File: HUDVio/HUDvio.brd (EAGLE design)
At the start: 85 x 54 mm, 53 parts, among them U1 ST_STM32F446RET7, U3 TVP5150AM1PBSR, U4 NEXPERIA_NVT2006, U5 MAXIM_MAX4389, X1 ABRACON_ABM8-27.000MHZ, X2 ABRACON_ABM8-14.31818MHZ

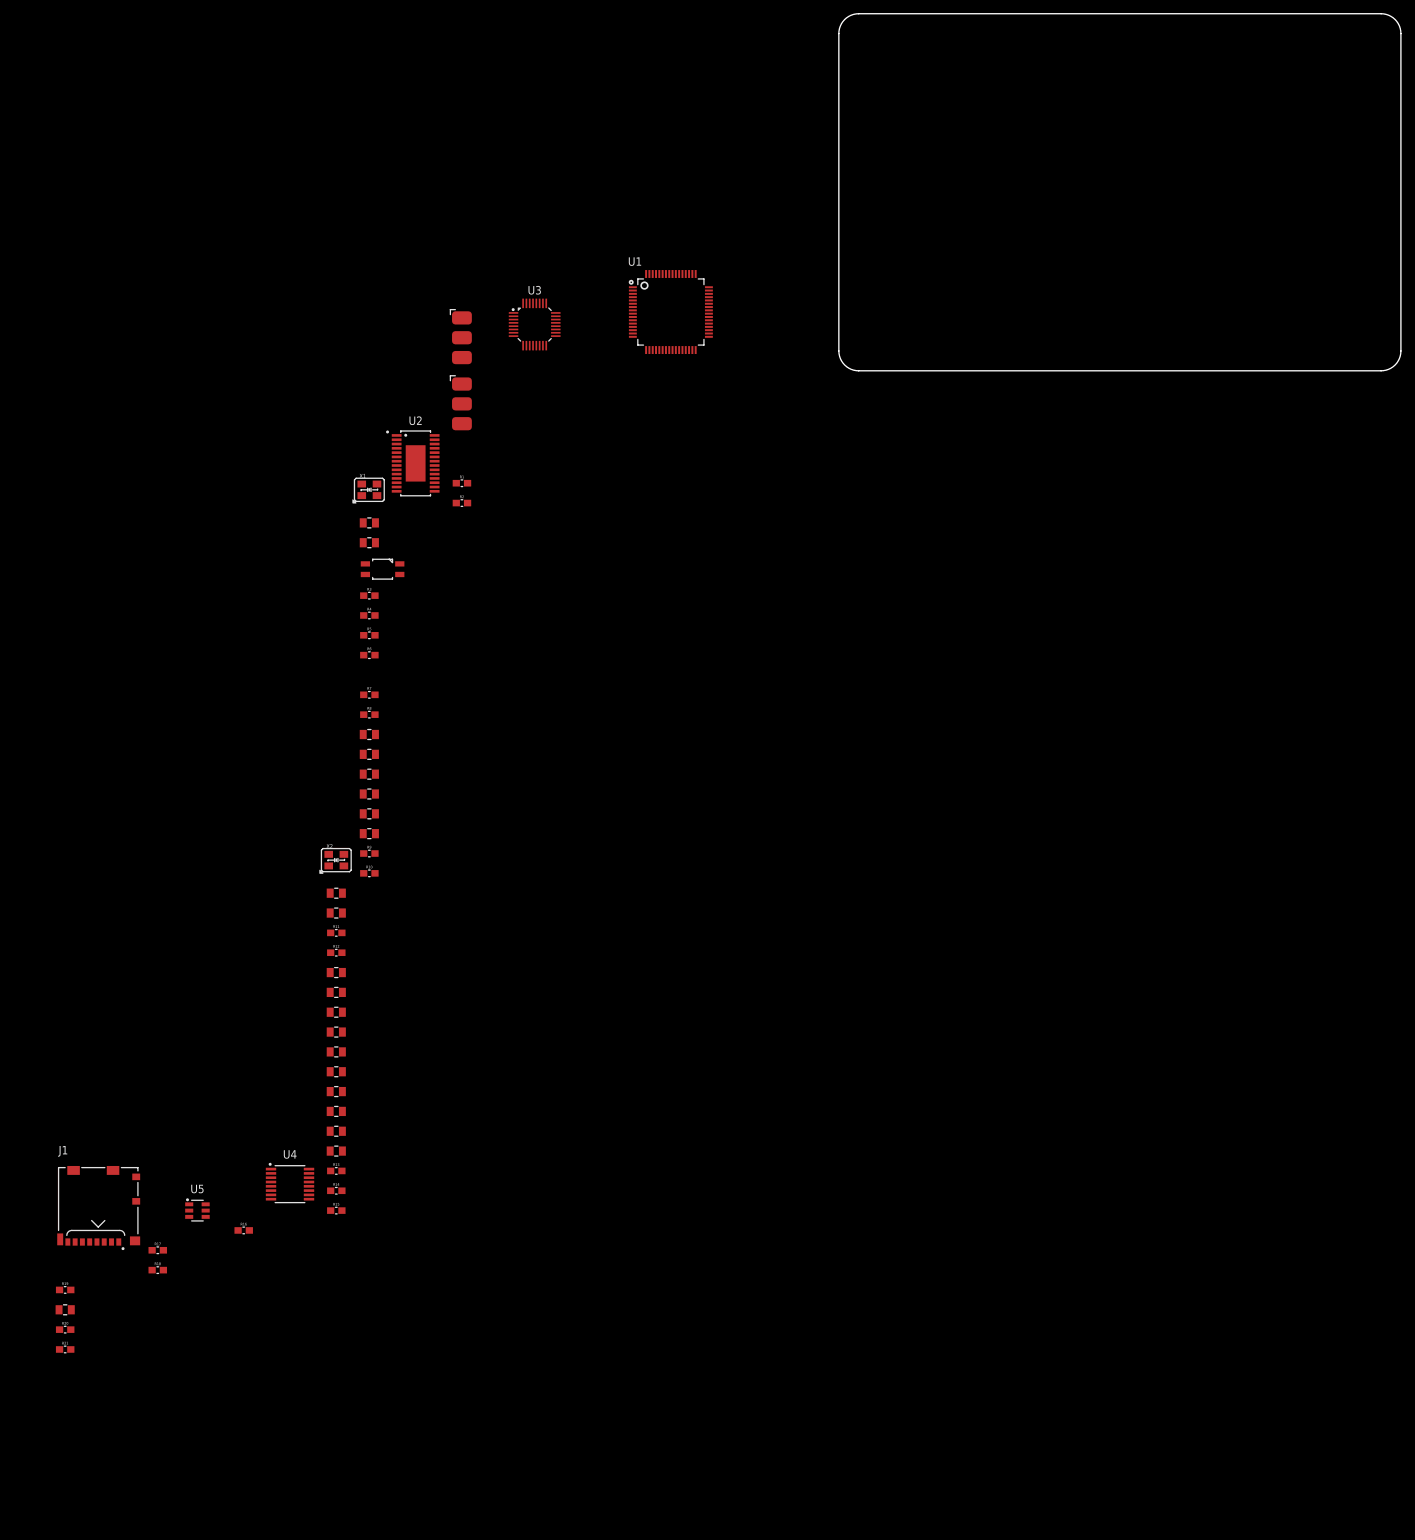
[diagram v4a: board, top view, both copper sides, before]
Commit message: Added 3rd sheet
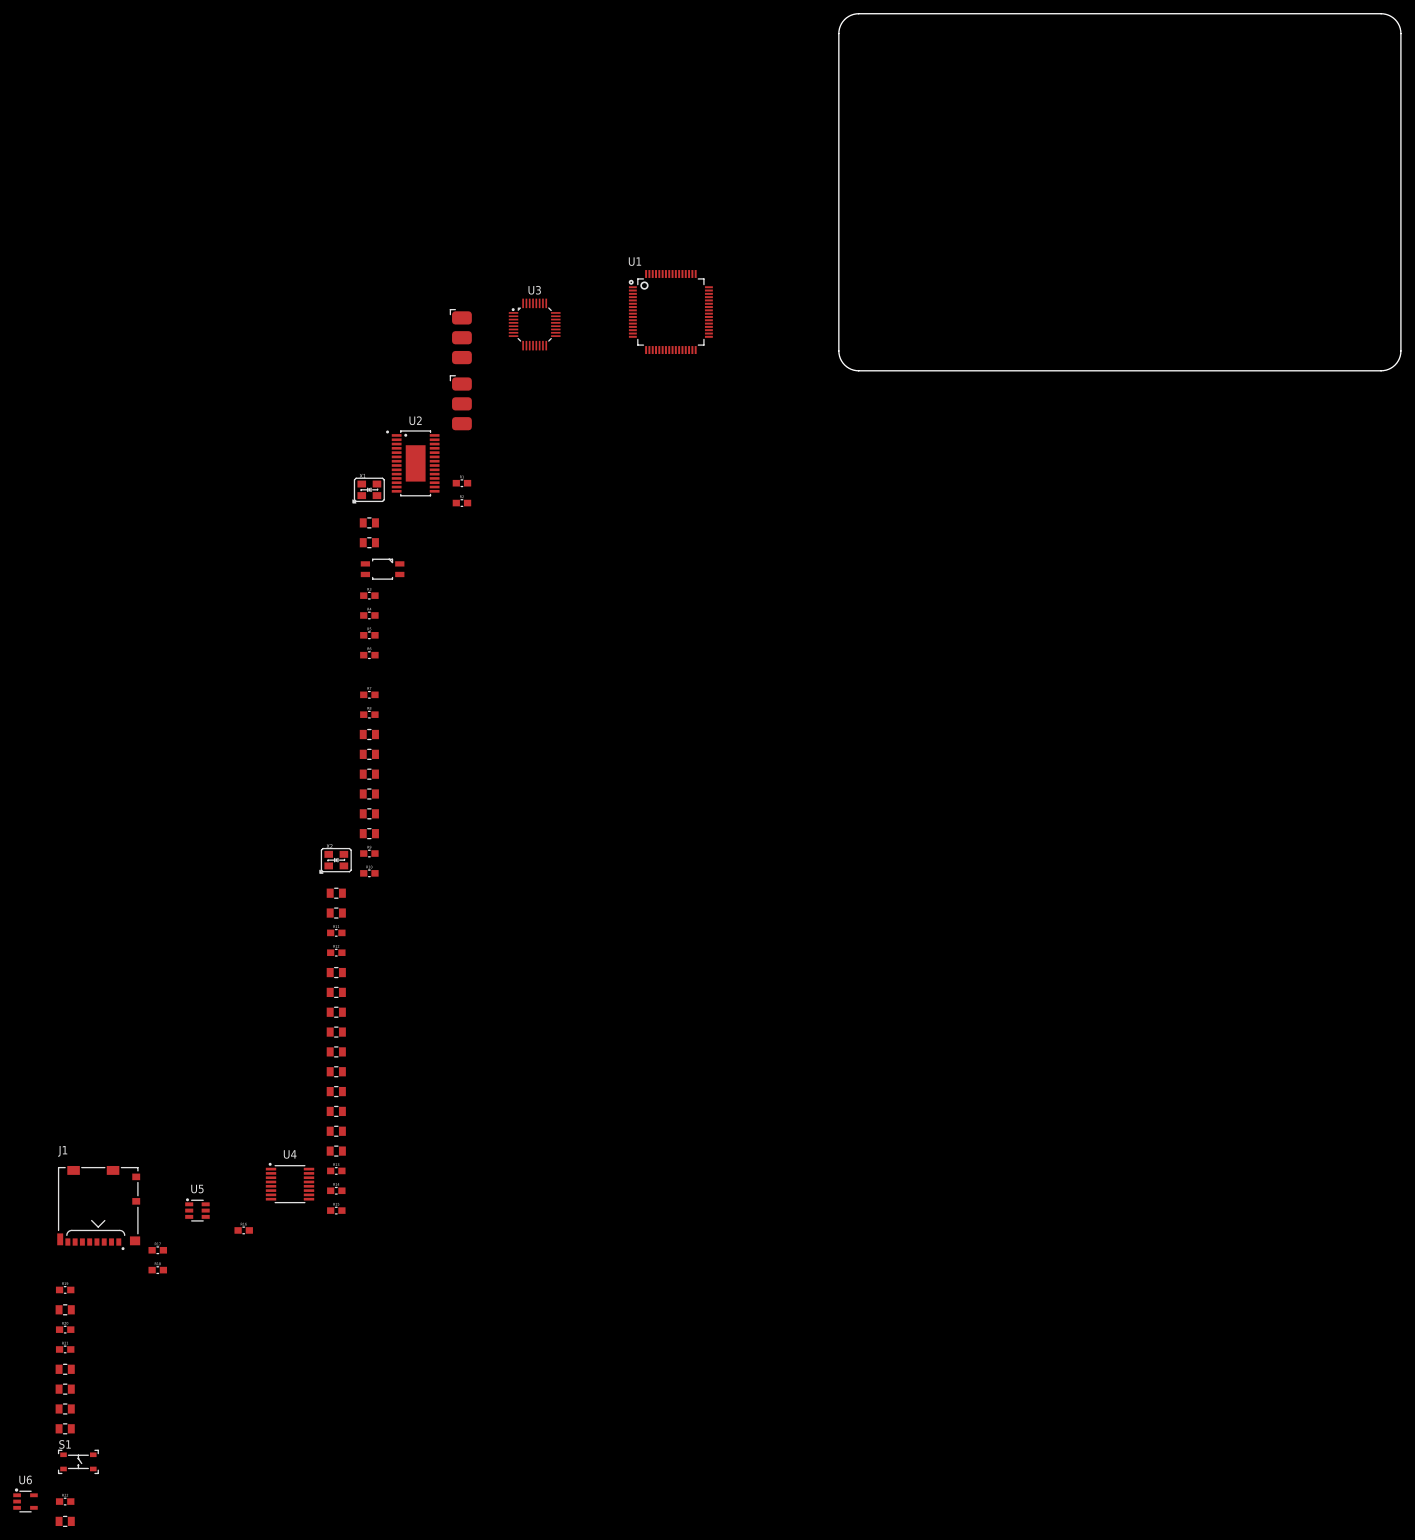
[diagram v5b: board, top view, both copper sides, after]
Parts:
- added C22, C23, C24, C25, C26: 1UF_0805, Skyhawkson-Capacitors:KEMET_0805
- added R22: 1K_0603, Skyhawkson-Resistors:0603
- added S1: C&K_PTS815, Skyhawkson-Miscellaneous:C&K_PTS815
- added U6: MIC_MIC5504-1.8, Skyhawkson-Power:MIC_SOT23-5LD-PL-1
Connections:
- removed net GNDA/VREF-: U1.12
- removed net VDD: U1.19, U1.32, U1.48, U1.64
- new net N$16: S1.2, U1.7
- new net N$17: R22.1, S1.1
- new net N$18: C26.P$2, S1.3
- new net VIN: U6.1
- new net VOUT: U6.5
- net +3V3: now also C22.P$1, C23.P$1, C24.P$1, C25.P$1, C26.P$1, R22.2, U1.13, U1.19, U1.32, U1.48, U1.64
- net 5150-CS: now also U1.33
- net BLU: now also U1.16
- net GND: now also C22.P$2, C23.P$2, C24.P$2, C25.P$2, S1.4, U1.12, U6.2
- net GRE: now also U1.15
- net LOS-LV: now also U1.8
- net MISO-LV: now also U1.35
- net MOSI-LV: now also U1.36
- net RED: now also U1.14
- net SCL: now also U1.29
- net SCLK-LV: now also U1.34
- net SD-CS: now also U1.56
- net SDA: now also U1.55
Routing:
- added copper zone on layer 2, net GND

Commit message: Schematic done, moving to Board
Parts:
- added C27, C28, C29, C30, C31, C32: 1UF_0805, Skyhawkson-Capacitors:KEMET_0805
- added J2: PHOENIX_SPTAF1/2-3,5, Skyhawkson-Connectors:PHOENIX_SPTAF1/X-3,5
- added U7: TOR_XC6220B331, Skyhawkson-Power:TOR_SOT-25
- added U8: ROHM_BD50HC5WEFJ, Skyhawkson-Power:ROHM_HTSOP-J8
- moved U$3 147.4 mm to (83.0, 41.0)
- moved U$1 69.1 mm to (2.00, 41.0)
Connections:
- removed net VIN: U6.1
- removed net VOUT: U6.5
- new net N$19: C29.P$1, C30.P$1, U7.2
- net +1V8: now also C28.P$2, U6.5
- net +3V3: now also C29.P$2, U7.5
- net +5V: now also C27.P$2, C30.P$2, C32.P$1, C32.P$2, U6.1, U6.3, U7.1, U7.3, U8.1, U8.2
- net GND: now also C27.P$1, C28.P$1, C31.P$1, C31.P$2, J2.1@BACK, J2.1@FRONT, J2.2@BACK, J2.2@FRONT, U8.3, U8.5, U8.8, U8.FIN, U8.FIN10, U8.FIN11, U8.FIN14, U8.FIN20, U8.FIN21, U8.FIN22, U8.FIN23, U8.FIN24, U8.FIN30, U8.FIN31, U8.FIN33, U8.FIN34

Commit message: Schematic Complete
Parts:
- added U$30: SWD_HEADER, Skyhawkson-Connectors:CNC_3220-10-0300-00
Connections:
- removed net N$16: S1.2, U1.7
- new net !RST: S1.2, U$30.10, U1.7
- new net SWCLK: U$30.4, U1.49
- new net SWDIO: U$30.2, U1.46
- net +3V3: now also U$30.1
- net GND: now also U$30.3, U$30.5, U$30.9
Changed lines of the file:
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@@
 <attribute name="VAL" value="1uF" x="-165" y="-192" size="1.778" layer="27" display="off"/>
+</element>
+<element name="U$30" library="Skyhawkson-Connectors" library_urn="urn:adsk.eagle:library:23896875" package="CNC_3220-10-0300-00" package3d_urn="urn:adsk.eagle:package:26105697/4" value="SWD_HEADER" x="-160" y="-199" smashed="yes">
+<attribute name="DKPN" value="1175-1629-ND" x="-160" y="-199" size="1.778" layer="27" display="off"/>
+<attribute name="NAME" x="-167" y="-195" size="1.27" layer="25"/>
+<attribute name="VALUE" x="-167" y="-203.5" size="1.27" layer="27" align="top-left"/>
 </element>
 </elements>
@@
 <contactref element="U8" pad="FIN33"/>
 <contactref element="C31" pad="P$2"/>
+<contactref element="U$30" pad="5"/>
+<contactref element="U$30" pad="3"/>
+<contactref element="U$30" pad="9"/>
 <wire x1="-114.395" y1="-131.75" x2="-117.755" y2="-131.35" width="0" layer="19" extent="1-1"/>
 <wire x1="-117.85" y1="-139" x2="-117.755" y2="-131.35" width="0" layer="19" extent="1-1"/>
@@
 <wire x1="-164.075" y1="-189" x2="-158.75" y2="-181.5" width="0" layer="19" extent="1-1"/>
 <wire x1="-165.925" y1="-189" x2="-164.075" y2="-189" width="0" layer="19" extent="1-1"/>
+<wire x1="-161.27" y1="-201.015" x2="-164.075" y2="-189" width="0" layer="19" extent="1-1"/>
+<wire x1="-160" y1="-201.015" x2="-161.27" y2="-201.015" width="0" layer="19" extent="1-1"/>
+<wire x1="-157.46" y1="-201.015" x2="-160" y2="-201.015" width="0" layer="19" extent="1-1"/>
 <wire x1="-70.075" y1="-26" x2="-70.15" y2="-49" width="0" layer="19" extent="1-1"/>
 <wire x1="-70.075" y1="-23" x2="-70.075" y2="-26" width="0" layer="19" extent="1-1"/>
@@
 <wire x1="-61.1265" y1="-13.025" x2="-66.8735" y2="-11.725" width="0" layer="19" extent="1-1"/>
 <wire x1="-61.1265" y1="-14.975" x2="-61.1265" y2="-13.025" width="0" layer="19" extent="1-1"/>
-<wire x1="83" y1="41" x2="-61.1265" y2="-13.025" width="0" layer="19" extent="1-1"/>
-<wire x1="2" y1="41" x2="83" y2="41" width="0" layer="19" extent="1-1"/>
-<wire x1="-49.1954" y1="5.75" x2="2" y2="41" width="0" layer="19" extent="1-1"/>
+<wire x1="-49.1954" y1="5.75" x2="-61.1265" y2="-13.025" width="0" layer="19" extent="1-1"/>
 <wire x1="-49.1954" y1="7.75" x2="-49.1954" y2="5.75" width="0" layer="19" extent="1-1"/>
 <wire x1="-47.25" y1="10.1954" x2="-49.1954" y2="7.75" width="0" layer="19" extent="1-1"/>
@@
 <wire x1="-28.65" y1="14.64" x2="-31.15" y2="7.14" width="0" layer="19" extent="1-1"/>
 <wire x1="-19.65" y1="12.14" x2="-22.15" y2="3.14" width="0" layer="19" extent="1-1"/>
+<wire x1="2" y1="41" x2="-19.65" y2="12.14" width="0" layer="19" extent="1-1"/>
+<wire x1="83" y1="41" x2="2" y2="41" width="0" layer="19" extent="1-1"/>
 </signal>
 <signal name="VCAP_1">
@@
 <contactref element="C29" pad="P$2"/>
 <contactref element="U7" pad="5"/>
+<contactref element="U$30" pad="1"/>
 <wire x1="-106.26" y1="-121.9" x2="-112.195" y2="-131.75" width="0" layer="19" extent="1-1"/>
 <wire x1="-116.15" y1="-145" x2="-112.195" y2="-131.75" width="0" layer="19" extent="1-1"/>
@@
 <wire x1="-75.075" y1="-100" x2="-85.8717" y2="-121.375" width="0" layer="19" extent="1-1"/>
 <wire x1="-76.85" y1="-85" x2="-75.075" y2="-100" width="0" layer="19" extent="1-1"/>
+<wire x1="-162.54" y1="-201.015" x2="-140.075" y2="-183" width="0" layer="19" extent="1-1"/>
 <wire x1="-47.25" y1="3.8046" x2="-76.85" y2="-85" width="0" layer="19" extent="1-1"/>
 <wire x1="-31.15" y1="6.64" x2="-47.25" y2="3.8046" width="0" layer="19" extent="1-1"/>
@@
 <wire x1="-25.15" y1="14.64" x2="-109.995" y2="-131.75" width="0" layer="19" extent="1-1"/>
 </signal>
-<signal name="N$16">
+<signal name="!RST">
 <contactref element="U1" pad="7"/>
 <contactref element="S1" pad="2"/>
-<wire x1="-112.75" y1="-163.925" x2="-31.15" y2="9.64" width="0" layer="19" extent="1-1"/>
+<contactref element="U$30" pad="10"/>
+<wire x1="-112.75" y1="-163.925" x2="-157.46" y2="-196.985" width="0" layer="19" extent="1-1"/>
+<wire x1="-31.15" y1="9.64" x2="-112.75" y2="-163.925" width="0" layer="19" extent="1-1"/>
 </signal>
 <signal name="N$17">
@@
 <wire x1="-136.2722" y1="-177" x2="-141.925" y2="-183" width="0" layer="19" extent="1-1"/>
 </signal>
+<signal name="SWCLK">
+<contactref element="U$30" pad="4"/>
+<contactref element="U1" pad="49"/>
+<wire x1="-21.65" y1="14.64" x2="-161.27" y2="-196.985" width="0" layer="19" extent="1-1"/>
+</signal>
+<signal name="SWDIO">
+<contactref element="U1" pad="46"/>
+<contactref element="U$30" pad="2"/>
+<wire x1="-19.65" y1="11.64" x2="-162.54" y2="-196.985" width="0" layer="19" extent="1-1"/>
+</signal>
 </signals>

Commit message: Started Layout
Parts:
- moved R13 181.8 mm to (7.50, 40.5), turned to 180 degrees
- moved C9 138.7 mm to (20.2, 34.5), turned to 180 degrees
- moved C8 138.2 mm to (11.0, 44.2)
- moved C4 131.8 mm to (16.5, 34.5)
- moved C7 130.5 mm to (11.0, 40.5), turned to 180 degrees
- moved R7 122.7 mm to (11.0, 42.2)
- moved C3 118.0 mm to (24.8, 43.0)
- moved C2 112.5 mm to (24.8, 36.0), turned to 180 degrees
- moved X1 111.7 mm to (24.8, 39.5), turned to 90 degrees
- moved U3 104.0 mm to (53.0, 39.0)
- moved U2 98.7 mm to (18.0, 41.0), turned to 180 degrees
- moved C21 18.7 mm to (-112.0, -124.0), turned to 270 degrees
- moved R19 15.0 mm to (-116.0, -124.0), turned to 90 degrees
- moved J1 13.3 mm to (-125.0, -129.0)
- moved U$1 2.50 mm to (2.00, 43.5)
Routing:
- net +5V: track 0.00 -> 17.5 mm, vias 0 -> 2
- net GND: track 0.00 -> 17.3 mm, vias 0 -> 9
- net CLKIN: track 0.00 -> 8.00 mm
- net XFB: track 0.00 -> 5.92 mm
- net VIDEO-IN: track 0.00 -> 4.65 mm
- net $NET11: track 0.00 -> 3.51 mm
- net VIDIN: track 0.00 -> 3.27 mm
